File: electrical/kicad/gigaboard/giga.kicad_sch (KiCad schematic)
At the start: 61 parts

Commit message: update(elec): readme
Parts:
- removed C? (x5): 100uF, Capacitor_THT:C_Radial_D4.0mm_H5.0mm_P1.50mm, symbol ControlPCB-rescue:CP1_Small
- removed C?: C, symbol Device:C
- removed D? (x5): TMC2209, TMC2209_SILENTSTEPSTICK:MODULE_TMC2209_SILENTSTEPSTICK, symbol Motor_Driver:TMC2209
- removed E? (x6): AS5600, symbol Sensors:AS5600_Encoder
- removed F?: Fuse, symbol Device:Fuse
- removed J? (x5): Conn_01x04, symbol Connector_Generic:Conn_01x04
- removed J? (x5): Conn_02x04_Counter_Clockwise, symbol Connector_Generic:Conn_02x04_Counter_Clockwise
- removed Q?: PMOS, symbol Simulation_SPICE:PMOS
- removed Q?: BS108, Package_TO_SOT_THT:TO-92_Inline, symbol Transistor_FET:BS108
- removed R? (x5): 10k, symbol Device:R
- removed R? (x5): 100k, symbol Device:R
- removed R?: R, symbol Device:R
- removed SW?: SW_DIP_x01, symbol Switch:SW_DIP_x01
- added C2, C3, C4, C5, C6: 100uF, symbol ControlPCB-rescue:CP1_Small
- added D2, D3, D4, D5, D6: TMC2209, symbol Motor_Driver:TMC2209
- added J10, J11, J12, J14, J20, J26, J5, J6: Conn_01x04, symbol Connector_Generic:Conn_01x04
- added J2, J3, J7, J8, J9: Conn_02x04_Counter_Clockwise, symbol Connector_Generic:Conn_02x04_Counter_Clockwise
- added J24: Conn_01x06, symbol Connector_Generic:Conn_01x06
- added R10, R11, R12, R5, R6: 10k, symbol Device:R
- added R2, R3, R7, R8, R9: 100k, symbol Device:R
- A1: renamed from A?; footprint MCU:Arduino_Giga_R1 -> MCU:Arduino_Giga-R1
- C1: renamed from C?; footprint Capacitor_THT:C_Radial_D4.0mm_H5.0mm_P1.50mm -> (none)
- D1: renamed from D?; footprint TMC2209_SILENTSTEPSTICK:MODULE_TMC2209_SILENTSTEPSTICK -> (none)
- U1: renamed from U?; footprint 2717:MODULE_2717 -> (none)
- gave numbers to parts that had none: 15
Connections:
- net E-STOP is gone; now on net DC1_DIR: A1.D23
- net +5V: now also J1.1 (Pin_1), J1.2 (Pin_2), J1.3 (Pin_3), D2.2 (VIO), D3.2 (VIO), D4.2 (VIO), D5.2 (VIO), D6.2 (VIO), J2.1 (Pin_1), J2.2 (Pin_2), J2.3 (Pin_3), J3.1 (Pin_1), J3.2 (Pin_2), J3.3 (Pin_3), J7.1 (Pin_1), J7.2 (Pin_2), J7.3 (Pin_3), J8.1 (Pin_1), J8.2 (Pin_2), J8.3 (Pin_3), J9.1 (Pin_1), J9.2 (Pin_2), J9.3 (Pin_3), R10.1, R11.1, R12.1, R5.1, R6.1
- net DC1_CHA: now also A1.D24; no longer A1.D31
- net DC1_CHB: now also A1.D25; no longer A1.D32
- net DC1_DIR: no longer A1.D30
- net DC2_CHA: now also A1.D27; no longer A1.D34
- net DC2_CHB: now also A1.D28; no longer A1.D35
- net DC2_DIR: now also A1.D26; no longer A1.D33
- net DC3_CHA: now also A1.D30; no longer A1.D37
- net DC3_CHB: now also A1.D31; no longer A1.D38
- net DC3_DIR: now also A1.D29; no longer A1.D36
- net DC4_CHA: now also A1.D33; no longer A1.D40
- net DC4_CHB: now also A1.D34; no longer A1.D41
- net DC4_DIR: now also A1.D32; no longer A1.D39
- net DC5_CHA: now also A1.D36; no longer A1.D43
- net DC5_CHB: now also A1.D37; no longer A1.D44
- net DC5_DIR: now also A1.D35; no longer A1.D42
- net DC6_CHA: now also A1.D39; no longer A1.D46
- net DC6_CHB: now also A1.D40; no longer A1.D47
- net DC6_DIR: now also A1.D38; no longer A1.D45
- net GND: now also C2.2, C3.2, C4.2, C5.2, C6.2, D2.1 (GND), D2.7 (GND), D3.1 (GND), D3.7 (GND), D4.1 (GND), D4.7 (GND), D5.1 (GND), D5.7 (GND), D6.1 (GND), D6.7 (GND), R2.2, R3.2, R7.2, R8.2, R9.2
- net ST1_DIR: now also A1.D43; no longer A1.D53
- net ST1_ENA: no longer A1.D51
- net ST1_STP: now also A1.D42; no longer A1.D52
- net ST2_DIR: now also A1.D45, D2.9 (DIR); no longer A1.D56
- net ST2_ENA: now also D2.16 (~{EN}), R5.2; no longer A1.D54
- net ST2_STP: now also A1.D44, D2.10 (STEP); no longer A1.D55
- net ST3_DIR: now also A1.D47, D3.9 (DIR); no longer A1.D59
- net ST3_ENA: now also D3.16 (~{EN}), R6.2; no longer A1.D57
- net ST3_STP: now also A1.D46, D3.10 (STEP); no longer A1.D58
- net ST4_DIR: now also A1.D49, D4.9 (DIR); no longer A1.D62
- net ST4_ENA: now also D4.16 (~{EN}), R10.2; no longer A1.D60
- net ST4_STP: now also A1.D48, D4.10 (STEP); no longer A1.D61
- net ST5_DIR: now also A1.D51, D5.9 (DIR); no longer A1.D65
- net ST5_ENA: now also D5.16 (~{EN}), R11.2; no longer A1.D63
- net ST5_STP: now also A1.D50, D5.10 (STEP); no longer A1.D64
- net ST6_DIR: now also A1.D53, D6.9 (DIR); no longer A1.D68
- net ST6_ENA: now also D6.16 (~{EN}), R12.2; no longer A1.D66
- net ST6_STP: now also A1.D52, D6.10 (STEP); no longer A1.D67
- net VM: now also C2.1, C3.1, C4.1, C5.1, C6.1, D2.8 (VM), D3.8 (VM), D4.8 (VM), D5.8 (VM), D6.8 (VM)
- net BAT1_S1: now reaches A1.A0
- net BAT1_S1: now also J14.1 (Pin_1)
- net BAT1_S2: now reaches A1.A1
- net BAT1_S2: now also J14.2 (Pin_2)
- net A10: now reaches A1.A10
- net A10: now also J26.3 (Pin_3)
- net A11: now reaches A1.A11
- net A11: now also J26.4 (Pin_4)
- net BAT1_S3: now reaches A1.A2
- net BAT1_S3: now also J14.3 (Pin_3)
- net BAT1_S4: now reaches A1.A3
- net BAT1_S4: now also J14.4 (Pin_4)
- net BAT2_S1: now reaches A1.A4
- net BAT2_S1: now also J20.1 (Pin_1)
- net BAT2_S2: now reaches A1.A5
- net BAT2_S2: now also J20.2 (Pin_2)
- net BAT2_S3: now reaches A1.A6
- net BAT2_S3: now also J20.3 (Pin_3)
- net BAT2_S4: now reaches A1.A7
- net BAT2_S4: now also J20.4 (Pin_4)
- net A8: now reaches A1.A8
- net A8: now also J26.1 (Pin_1)
- net A9: now reaches A1.A9
- net A9: now also J26.2 (Pin_2)
- net BAT_MAX: now reaches A1.AREF
- net TX3: now reaches A1.D14 (D14/TX3)
- net TX3: now also J24.4 (Pin_4)
- net RX3: now reaches A1.D15 (D15/RX3)
- net RX3: now also J24.3 (Pin_3)
- net TX2: now reaches A1.D16 (D16/TX2)
- net TX2: now also J24.2 (Pin_2)
- net RX2: now reaches A1.D17 (D17/RX2)
- net RX2: now also J24.1 (Pin_1)
- net SCL: now reaches A1.D8 (D8/SCL2)
- net SCL: now also J24.5 (Pin_5)
- net SDA: now reaches A1.D9 (D9/SDA2)
- net SDA: now also J24.6 (Pin_6)
- net GIGA_EN: now reaches A1.OFF
- net GIGA_RST: now reaches A1.RST1 (RESET)
- net ST1_URT: no longer names the net of J1.4 (Pin_4)
- removed net STP_MS1: A1.D48, J1.1 (Pin_1)
- removed net STP_MS2: A1.D49, J1.2 (Pin_2)
- removed net STP_MS3: A1.D50, J1.3 (Pin_3)
- new net: D3.15 (MS1), J3.8 (Pin_8), R3.1
- new net: D3.11 (PDN), D3.12 (UART), J3.5 (Pin_5)
- new net: D3.13 (SPRD), J3.6 (Pin_6)
- new net: D3.14 (MS2), J3.7 (Pin_7)
- new net: D3.3 (1B), J6.4 (Pin_4)
- new net: D3.4 (1A), J6.3 (Pin_3)
- new net: D3.5 (2A), J6.2 (Pin_2)
- new net: D3.6 (2B), J6.1 (Pin_1)
- new net: D5.15 (MS1), J8.8 (Pin_8), R8.1
- new net: D5.6 (2B), J11.1 (Pin_1)
- new net: D5.5 (2A), J11.2 (Pin_2)
- new net: D5.4 (1A), J11.3 (Pin_3)
- new net: D5.3 (1B), J11.4 (Pin_4)
- new net: D6.15 (MS1), J9.8 (Pin_8), R9.1
- new net: D2.6 (2B), J5.1 (Pin_1)
- new net: D2.5 (2A), J5.2 (Pin_2)
- new net: D2.4 (1A), J5.3 (Pin_3)
- new net: D2.3 (1B), J5.4 (Pin_4)
- new net: D6.6 (2B), J12.1 (Pin_1)
- new net: D6.5 (2A), J12.2 (Pin_2)
- new net: D6.4 (1A), J12.3 (Pin_3)
- new net: D6.3 (1B), J12.4 (Pin_4)
- new net: D2.15 (MS1), J2.8 (Pin_8), R2.1
- new net: D4.11 (PDN), D4.12 (UART), J7.5 (Pin_5)
- new net: D4.13 (SPRD), J7.6 (Pin_6)
- new net: D4.14 (MS2), J7.7 (Pin_7)
- new net: D4.15 (MS1), J7.8 (Pin_8), R7.1
- new net: D4.3 (1B), J10.4 (Pin_4)
- new net: D4.4 (1A), J10.3 (Pin_3)
- new net: D4.5 (2A), J10.2 (Pin_2)
- new net: D4.6 (2B), J10.1 (Pin_1)
- new net: D2.11 (PDN), D2.12 (UART), J2.5 (Pin_5)
- new net: D2.13 (SPRD), J2.6 (Pin_6)
- new net: D2.14 (MS2), J2.7 (Pin_7)
- new net: D5.11 (PDN), D5.12 (UART), J8.5 (Pin_5)
- new net: D5.13 (SPRD), J8.6 (Pin_6)
- new net: D5.14 (MS2), J8.7 (Pin_7)
- new net: D6.11 (PDN), D6.12 (UART), J9.5 (Pin_5)
- new net: D6.13 (SPRD), J9.6 (Pin_6)
- new net: D6.14 (MS2), J9.7 (Pin_7)
- new net STP_ENA: A1.D41
- no-connect marks 25 -> 64
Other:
- moved on the sheet: C1, D1, J1, J13, J15, J16, J17, J18, J19, J21, J22, J23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

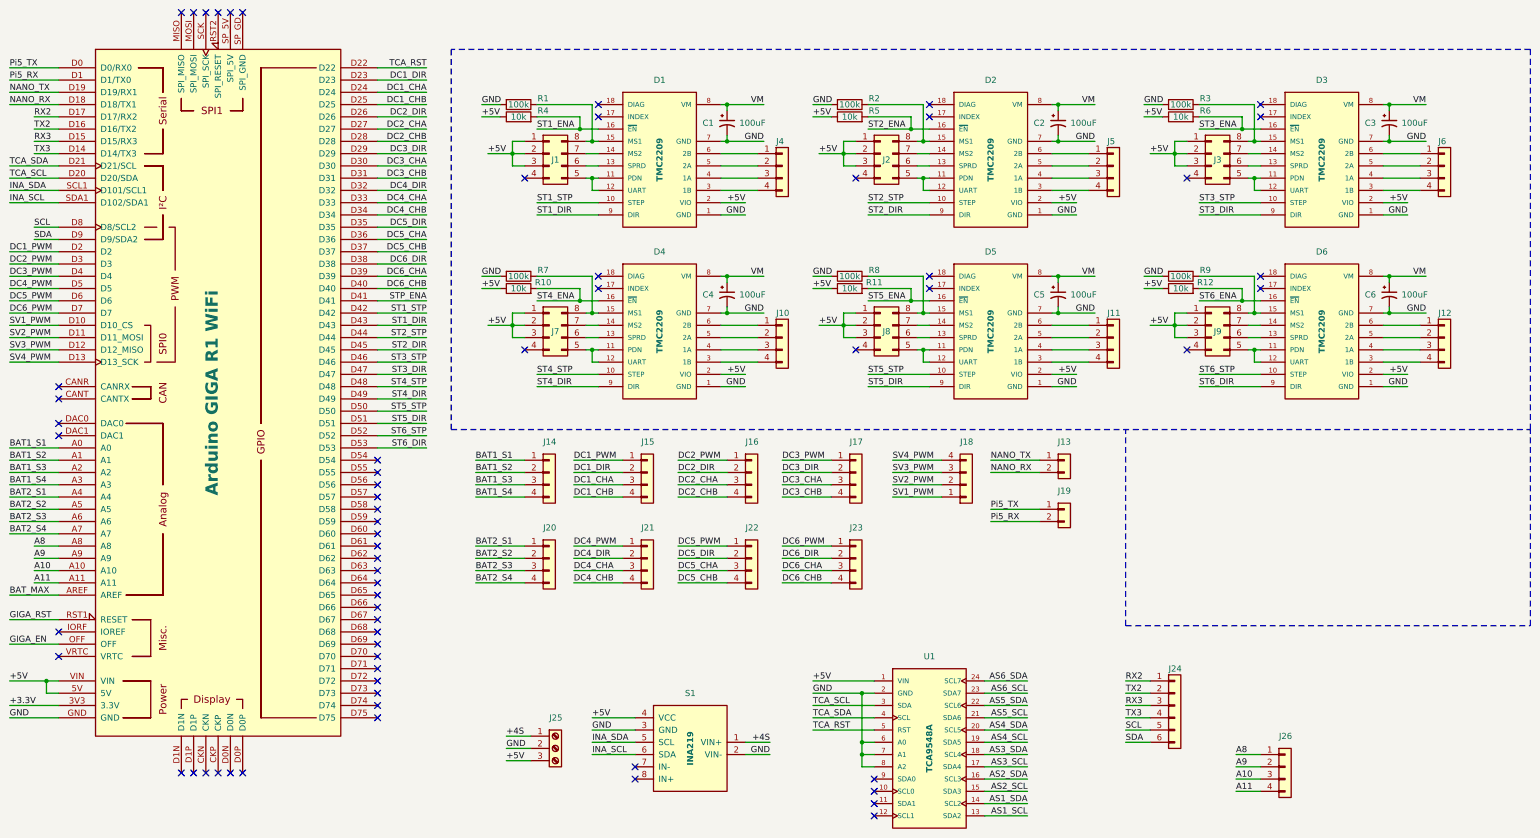
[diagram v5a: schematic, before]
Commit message: update(giga): sch complete (ERC Passed)
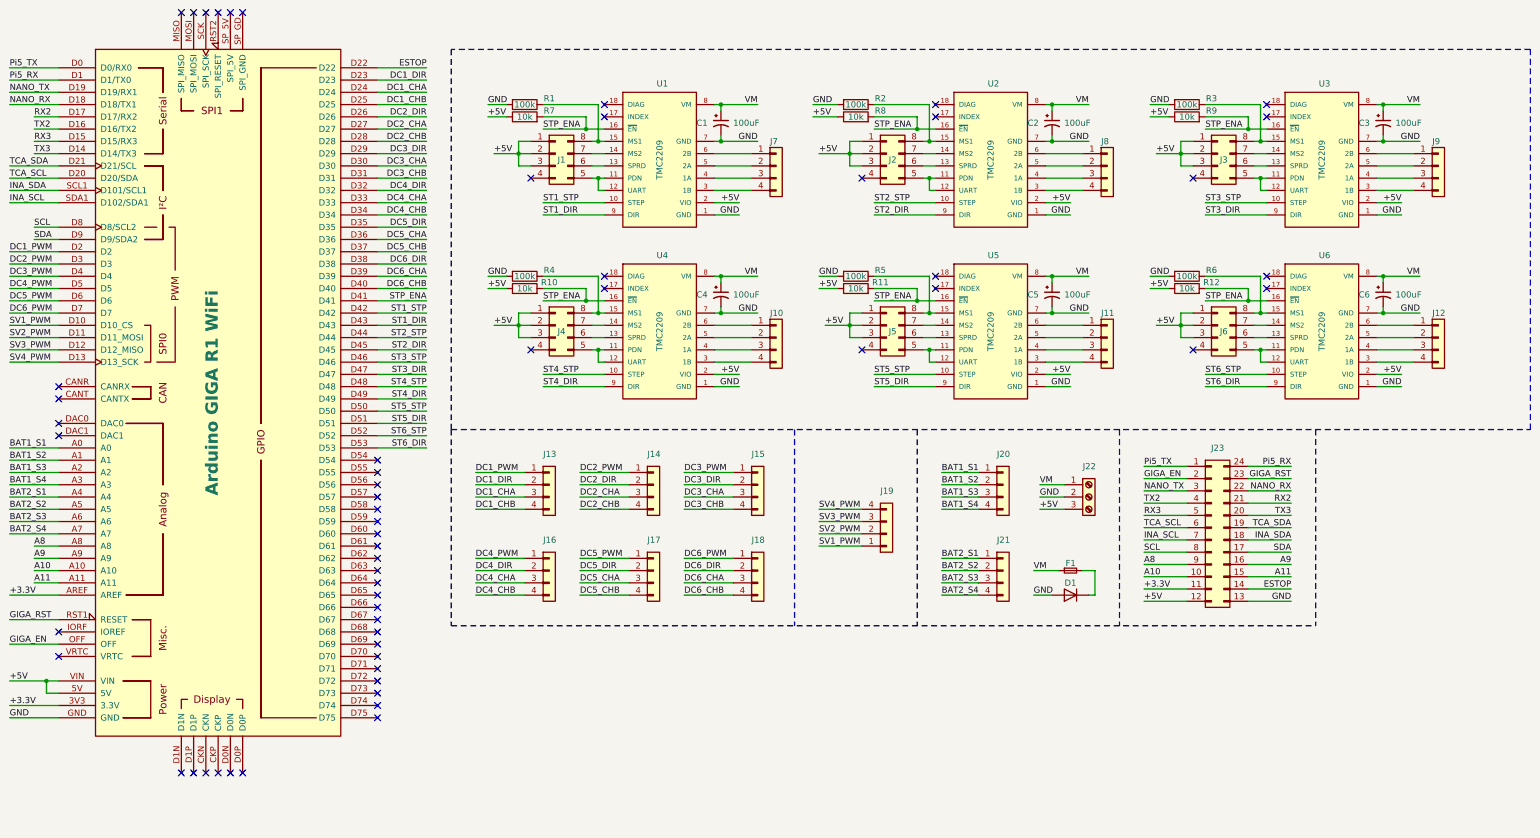
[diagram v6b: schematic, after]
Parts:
- removed C1: 100uF, symbol ControlPCB-rescue:CP1_Small
- removed J13, J19: Conn_01x02, symbol Connector_Generic:Conn_01x02
- removed J14, J26, J4: Conn_01x04, symbol Connector_Generic:Conn_01x04
- removed J24: Conn_01x06, symbol Connector_Generic:Conn_01x06
- removed J25: Screw_Terminal_01x03, symbol Connector:Screw_Terminal_01x03
- removed S1: INA219, symbol Sensors:INA219_Current_Voltage_Sensor
- removed U1: TCA9548A, symbol Comms:TCA9548A
- added C1: 100uF, Capacitor_SMD:CP_Elec_6.3x7.7, symbol Device:C_Polarized_Small_US
- added D1: D, Diode_THT:D_DO-35_SOD27_P7.62mm_Horizontal, symbol Device:D
- added F1: F_Small, Fuse:Fuseholder_Blade_Mini_Keystone_3568, symbol Device:Fuse_Small
- added J21, J7: Conn_01x04, Connector_PinSocket_2.54mm:PinSocket_1x04_P2.54mm_Vertical, symbol Connector_Generic:Conn_01x04
- added J22: Screw_Terminal_01x03, Connector_Phoenix_MSTB:PhoenixContact_MSTBA_2,5_3-G-5,08_1x03_P5.08mm_Horizontal, symbol Connector:Screw_Terminal_01x03
- added J23: Conn_02x12_Counter_Clockwise, Connector_PinSocket_2.54mm:PinSocket_2x12_P2.54mm_Vertical, symbol Connector_Generic:Conn_02x12_Counter_Clockwise
- C2, C3, C4, C5, C6: footprint (none) -> Capacitor_SMD:CP_Elec_6.3x7.7; symbol ControlPCB-rescue:CP1_Small -> Device:C_Polarized_Small_US
- J1, J2, J3: footprint (none) -> Connector_PinSocket_2.54mm:PinSocket_2x04_P2.54mm_Vertical
- J10, J11, J12, J20: footprint (none) -> Connector_PinSocket_2.54mm:PinSocket_1x04_P2.54mm_Vertical
- J13: renamed from J15; footprint (none) -> Connector_PinSocket_2.54mm:PinSocket_1x04_P2.54mm_Vertical
- J14: renamed from J16; footprint (none) -> Connector_PinSocket_2.54mm:PinSocket_1x04_P2.54mm_Vertical
- J15: renamed from J17; footprint (none) -> Connector_PinSocket_2.54mm:PinSocket_1x04_P2.54mm_Vertical
- J16: renamed from J21; footprint (none) -> Connector_PinSocket_2.54mm:PinSocket_1x04_P2.54mm_Vertical
- J17: renamed from J22; footprint (none) -> Connector_PinSocket_2.54mm:PinSocket_1x04_P2.54mm_Vertical
- J18: renamed from J23; footprint (none) -> Connector_PinSocket_2.54mm:PinSocket_1x04_P2.54mm_Vertical
- J19: renamed from J18; footprint (none) -> Connector_PinSocket_2.54mm:PinSocket_1x04_P2.54mm_Vertical
- J4: renamed from J7; footprint (none) -> Connector_PinSocket_2.54mm:PinSocket_2x04_P2.54mm_Vertical
- J5: renamed from J8; footprint (none) -> Connector_PinSocket_2.54mm:PinSocket_2x04_P2.54mm_Vertical
- J6: renamed from J9; footprint (none) -> Connector_PinSocket_2.54mm:PinSocket_2x04_P2.54mm_Vertical
- J8: renamed from J5; footprint (none) -> Connector_PinSocket_2.54mm:PinSocket_1x04_P2.54mm_Vertical
- J9: renamed from J6; footprint (none) -> Connector_PinSocket_2.54mm:PinSocket_1x04_P2.54mm_Vertical
- R1, R10, R11, R12, R2, R3: footprint (none) -> Resistor_THT:R_Axial_DIN0207_L6.3mm_D2.5mm_P7.62mm_Horizontal
- R4: renamed from R7; footprint (none) -> Resistor_THT:R_Axial_DIN0207_L6.3mm_D2.5mm_P7.62mm_Horizontal
- R5: renamed from R8; footprint (none) -> Resistor_THT:R_Axial_DIN0207_L6.3mm_D2.5mm_P7.62mm_Horizontal
- R6: renamed from R9; footprint (none) -> Resistor_THT:R_Axial_DIN0207_L6.3mm_D2.5mm_P7.62mm_Horizontal
- R7: renamed from R4; footprint (none) -> Resistor_THT:R_Axial_DIN0207_L6.3mm_D2.5mm_P7.62mm_Horizontal
- R8: renamed from R5; footprint (none) -> Resistor_THT:R_Axial_DIN0207_L6.3mm_D2.5mm_P7.62mm_Horizontal
- R9: renamed from R6; footprint (none) -> Resistor_THT:R_Axial_DIN0207_L6.3mm_D2.5mm_P7.62mm_Horizontal
- U1: renamed from D1; footprint (none) -> Motor_Driver:MKS_TMC2209; symbol Motor_Driver:TMC2209 -> Motor_Driver:TMC2209_Stepper_Driver; MANUFACTURER Trinamic Motion Control GmbH -> (none); PARTREV 1.20 -> (none); SnapEDA (none) -> https://www.snapeda.com/parts/TMC2209%20SILENTSTEPSTICK/Tri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; SnapEDA_Link https://www.snapeda.com/parts/TMC2209%20SILENTSTEPSTICK/Tri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 -> (none)
- U2: renamed from D2; footprint (none) -> Motor_Driver:MKS_TMC2209; symbol Motor_Driver:TMC2209 -> Motor_Driver:TMC2209_Stepper_Driver; MANUFACTURER Trinamic Motion Control GmbH -> (none); PARTREV 1.20 -> (none); SnapEDA (none) -> https://www.snapeda.com/parts/TMC2209%20SILENTSTEPSTICK/Tri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; SnapEDA_Link https://www.snapeda.com/parts/TMC2209%20SILENTSTEPSTICK/Tri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 -> (none)
- U3: renamed from D3; footprint (none) -> Motor_Driver:MKS_TMC2209; symbol Motor_Driver:TMC2209 -> Motor_Driver:TMC2209_Stepper_Driver; MANUFACTURER Trinamic Motion Control GmbH -> (none); PARTREV 1.20 -> (none); SnapEDA (none) -> https://www.snapeda.com/parts/TMC2209%20SILENTSTEPSTICK/Tri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; SnapEDA_Link https://www.snapeda.com/parts/TMC2209%20SILENTSTEPSTICK/Tri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 -> (none)
- U4: renamed from D4; footprint (none) -> Motor_Driver:MKS_TMC2209; symbol Motor_Driver:TMC2209 -> Motor_Driver:TMC2209_Stepper_Driver; MANUFACTURER Trinamic Motion Control GmbH -> (none); PARTREV 1.20 -> (none); SnapEDA (none) -> https://www.snapeda.com/parts/TMC2209%20SILENTSTEPSTICK/Tri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; SnapEDA_Link https://www.snapeda.com/parts/TMC2209%20SILENTSTEPSTICK/Tri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 -> (none)
- U5: renamed from D5; footprint (none) -> Motor_Driver:MKS_TMC2209; symbol Motor_Driver:TMC2209 -> Motor_Driver:TMC2209_Stepper_Driver; MANUFACTURER Trinamic Motion Control GmbH -> (none); PARTREV 1.20 -> (none); SnapEDA (none) -> https://www.snapeda.com/parts/TMC2209%20SILENTSTEPSTICK/Tri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; SnapEDA_Link https://www.snapeda.com/parts/TMC2209%20SILENTSTEPSTICK/Tri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 -> (none)
- U6: renamed from D6; footprint (none) -> Motor_Driver:MKS_TMC2209; symbol Motor_Driver:TMC2209 -> Motor_Driver:TMC2209_Stepper_Driver; MANUFACTURER Trinamic Motion Control GmbH -> (none); PARTREV 1.20 -> (none); SnapEDA (none) -> https://www.snapeda.com/parts/TMC2209%20SILENTSTEPSTICK/Tri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; SnapEDA_Link https://www.snapeda.com/parts/TMC2209%20SILENTSTEPSTICK/Tri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 -> (none)
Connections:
- net BAT_MAX is gone; now on net +3.3V: A1.AREF
- net ST1_ENA is gone; now on net STP_ENA: R7.2, U1.16 (~{EN})
- net ST2_ENA is gone; now on net STP_ENA: R8.2, U2.16 (~{EN})
- net ST3_ENA is gone; now on net STP_ENA: R9.2, U3.16 (~{EN})
- net ST4_ENA is gone; now on net STP_ENA: R10.2, U4.16 (~{EN})
- net ST5_ENA is gone; now on net STP_ENA: R11.2, U5.16 (~{EN})
- net ST6_ENA is gone; now on net STP_ENA: R12.2, U6.16 (~{EN})
- net +3.3V: now also J23.11 (Pin_11)
- net +5V: now also J22.3 (Pin_3), J23.12 (Pin_12)
- net A10: now also J23.10 (Pin_10)
- net A11: now also J23.15 (Pin_15)
- net A8: now also J23.9 (Pin_9)
- net A9: now also J23.16 (Pin_16)
- net BAT1_S1: now also J20.1 (Pin_1)
- net BAT1_S2: now also J20.2 (Pin_2)
- net BAT1_S3: now also J20.3 (Pin_3)
- net BAT1_S4: now also J20.4 (Pin_4)
- net BAT2_S1: now also J21.1 (Pin_1); no longer J20.1 (Pin_1)
- net BAT2_S2: now also J21.2 (Pin_2); no longer J20.2 (Pin_2)
- net BAT2_S3: now also J21.3 (Pin_3); no longer J20.3 (Pin_3)
- net BAT2_S4: now also J21.4 (Pin_4); no longer J20.4 (Pin_4)
- net GIGA_EN: now also J23.2 (Pin_2)
- net GIGA_RST: now also J23.23 (Pin_23)
- net GND: now also C1.2, D1.2 (A), J22.2 (Pin_2), J23.13 (Pin_13)
- net INA_SCL: now also J23.7 (Pin_7)
- net INA_SDA: now also J23.18 (Pin_18)
- net NANO_RX: now also J23.22 (Pin_22)
- net NANO_TX: now also J23.3 (Pin_3)
- net Pi5_RX: now also J23.24 (Pin_24)
- net Pi5_TX: now also J23.1 (Pin_1)
- net RX2: now also J23.21 (Pin_21)
- net RX3: now also J23.5 (Pin_5)
- net SCL: now also J23.8 (Pin_8)
- net SDA: now also J23.17 (Pin_17)
- net TCA_SCL: now also J23.6 (Pin_6)
- net TCA_SDA: now also J23.19 (Pin_19)
- net TX2: now also J23.4 (Pin_4)
- net TX3: now also J23.20 (Pin_20)
- net VM: now also C1.1, F1.1, J22.1 (Pin_1)
- net at U1.6 (2B): now also J7.1 (Pin_1)
- net at U1.5 (2A): now also J7.2 (Pin_2)
- net at U1.4 (1A): now also J7.3 (Pin_3)
- net at U1.3 (1B): now also J7.4 (Pin_4)
- net TCA_RST renamed ESTOP
- net ESTOP: now also J23.14 (Pin_14)
- new net: D1.1 (K), F1.2
- no-connect marks 64 -> 58
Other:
- moved on the sheet: C2, C3, C4, C5, C6, J1, J10, J11, J12, J13, J14, J15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

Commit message: update(giga): pcb layout #02
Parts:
- removed J1: Conn_02x04_Counter_Clockwise, Connector_PinSocket_2.54mm:PinSocket_2x04_P2.54mm_Vertical, symbol Connector_Generic:Conn_02x04_Counter_Clockwise
- added J1: Conn_02x03_Counter_Clockwise, Connector_PinHeader_2.54mm:PinHeader_2x03_P2.54mm_Vertical, symbol Connector_Generic:Conn_02x03_Odd_Even
- J10, J11, J12, J13, J14, J15, J16, J17, J18, J19, J20, J21, J7, J8, J9: footprint Connector_PinSocket_2.54mm:PinSocket_1x04_P2.54mm_Vertical -> Connector_PinHeader_2.54mm:PinHeader_1x04_P2.54mm_Vertical
- J2, J3, J4, J5, J6: footprint Connector_PinSocket_2.54mm:PinSocket_2x04_P2.54mm_Vertical -> Connector_PinHeader_2.54mm:PinHeader_2x03_P2.54mm_Vertical; symbol Connector_Generic:Conn_02x04_Counter_Clockwise -> Connector_Generic:Conn_02x03_Odd_Even
- J23: footprint Connector_PinSocket_2.54mm:PinSocket_2x12_P2.54mm_Vertical -> Connector_PinHeader_2.54mm:PinHeader_2x12_P2.54mm_Vertical
- R1, R10, R11, R12, R2, R3, R4, R5, R6, R7, R8, R9: footprint Resistor_THT:R_Axial_DIN0207_L6.3mm_D2.5mm_P7.62mm_Horizontal -> Resistor_SMD:R_1206_3216Metric_Pad1.30x1.75mm_HandSolder
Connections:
- net +5V: now also J2.5 (Pin_5), J3.5 (Pin_5), J4.5 (Pin_5), J5.5 (Pin_5), J6.5 (Pin_5), J1.1 (Pin_1), J1.3 (Pin_3), J1.5 (Pin_5); no longer J2.2 (Pin_2), J3.2 (Pin_2), J4.2 (Pin_2), J5.2 (Pin_2), J6.2 (Pin_2)
- net at R3.1, U3.15 (MS1): now also J3.2 (Pin_2); no longer J3.8 (Pin_8)
- net at U3.14 (MS2): now also J3.4 (Pin_4); no longer J3.7 (Pin_7)
- net at R5.1, U5.15 (MS1): now also J5.2 (Pin_2); no longer J5.8 (Pin_8)
- net at R6.1, U6.15 (MS1): now also J6.2 (Pin_2); no longer J6.8 (Pin_8)
- net at R2.1, U2.15 (MS1): now also J2.2 (Pin_2); no longer J2.8 (Pin_8)
- net at U4.14 (MS2): now also J4.4 (Pin_4); no longer J4.7 (Pin_7)
- net at R4.1, U4.15 (MS1): now also J4.2 (Pin_2); no longer J4.8 (Pin_8)
- net at U2.14 (MS2): now also J2.4 (Pin_4); no longer J2.7 (Pin_7)
- net at U5.14 (MS2): now also J5.4 (Pin_4); no longer J5.7 (Pin_7)
- net at R1.1, U1.15 (MS1): now also J1.2 (Pin_2)
- net at J6.4 (Pin_4): now also U6.14 (MS2)
- net at U1.11 (PDN): no longer U1.12 (UART)
- net at U1.13 (SPRD): now also J1.6 (Pin_6)
- net at U1.14 (MS2): now also J1.4 (Pin_4)
- now unconnected: U2.11 (PDN), U2.12 (UART), U3.11 (PDN), U3.12 (UART), U4.11 (PDN), U4.12 (UART), U5.11 (PDN), U5.12 (UART), U6.11 (PDN), U6.12 (UART)
- no-connect marks 58 -> 52
